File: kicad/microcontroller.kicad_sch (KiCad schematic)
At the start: 26 parts, among them Q701 DMG1012T, U701 MLPF-WB55-01E3, U702 STM32WB55RGVx, Y701 32M

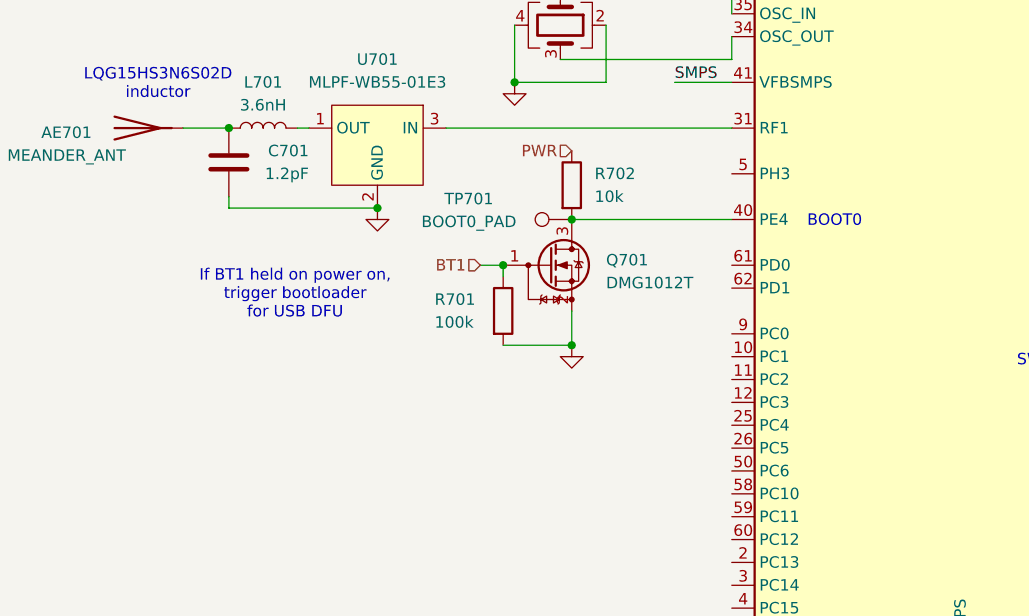
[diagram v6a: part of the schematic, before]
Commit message: Update BOOT0
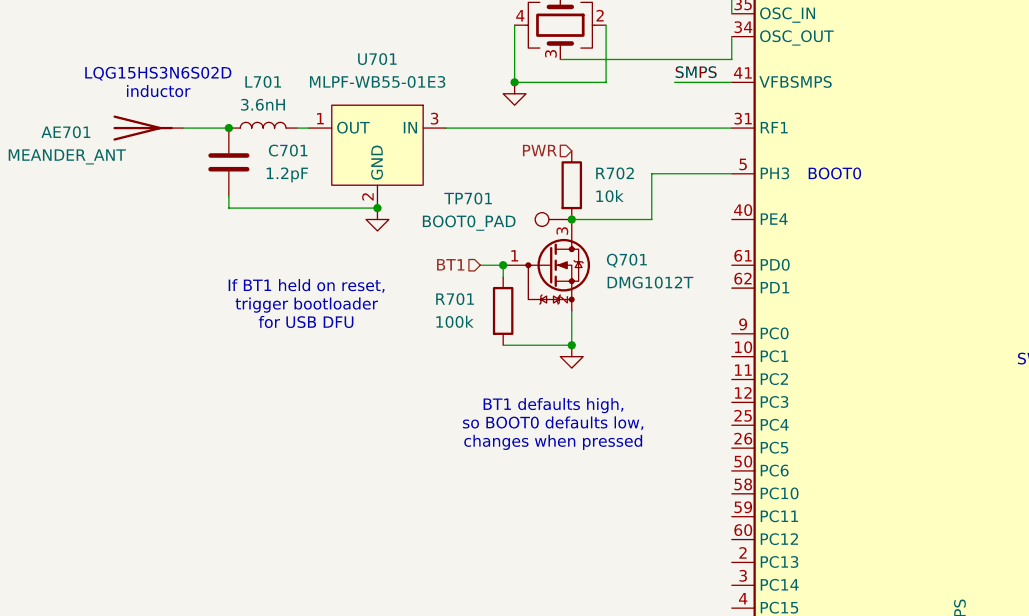
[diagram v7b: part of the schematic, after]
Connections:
- net at Q701.3 (D), R702.2, TP701.1: now also U702.5 (PH3); no longer U702.40 (PE4)
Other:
- note added: "BT1 defaults high, so BOOT0 defaults low, changes when pressed"
- note added: "If BT1 held on reset, trigger bootloader for USB DFU"
- note removed: "If BT1 held on power on, trigger bootloader for USB DFU"
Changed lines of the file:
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@@
+	(wire
+		(pts
+			(xy 106.68 104.14) (xy 106.68 109.22)
+		)
+		(stroke
+			(width 0)
+			(type default)
+		)
+	)
 	(wire
 		(pts
@@
 	(wire
 		(pts
-			(xy 97.79 109.22) (xy 115.57 109.22)
-		)
-		(stroke
-			(width 0)
-			(type default)
-		)
-	)
-	(wire
-		(pts
 			(xy 109.22 78.74) (xy 115.57 78.74)
 		)
@@
 	(wire
 		(pts
+			(xy 115.57 104.14) (xy 106.68 104.14)
+		)
+		(stroke
+			(width 0)
+			(type default)
+		)
+	)
+	(wire
+		(pts
 			(xy 158.75 119.38) (xy 162.56 119.38)
 		)
@@
 	(wire
 		(pts
+			(xy 106.68 109.22) (xy 97.79 109.22)
+		)
+		(stroke
+			(width 0)
+			(type default)
+		)
+	)
+	(wire
+		(pts
 			(xy 82.55 71.12) (xy 76.2 71.12)
 		)
@@
 		)
 	)
-	(text "LQG15HS3N6S02D\ninductor\n"
-		(exclude_from_sim no)
-		(at 51.816 94.234 0)
+	(text "BT1 defaults high,\nso BOOT0 defaults low,\nchanges when pressed"
+		(exclude_from_sim no)
+		(at 95.758 132.08 0)
 		(effects
 			(font
@@
 		)
 	)
-	(text "If BT1 held on power on,\ntrigger bootloader\nfor USB DFU"
-		(exclude_from_sim no)
-		(at 67.056 117.602 0)
+	(text "LQG15HS3N6S02D\ninductor\n"
+		(exclude_from_sim no)
+		(at 51.816 94.234 0)
 		(effects
 			(font
@@
 		)
 	)
-	(text "SWO"
-		(exclude_from_sim no)
-		(at 149.352 124.968 0)
+	(text "If BT1 held on reset,\ntrigger bootloader\nfor USB DFU"
+		(exclude_from_sim no)
+		(at 68.326 118.872 0)
 		(effects
 			(font
@@
 		)
 	)
-	(text "LRA PWM"
-		(exclude_from_sim no)
-		(at 180.594 73.914 0)
+	(text "SWO"
+		(exclude_from_sim no)
+		(at 149.352 124.968 0)
 		(effects
 			(font
@@
 		)
 	)
-	(text "SPI1:\nE-Ink display"
-		(exclude_from_sim no)
-		(at 183.642 88.138 0)
+	(text "LRA PWM"
+		(exclude_from_sim no)
+		(at 180.594 73.914 0)
 		(effects
 			(font
@@
 		)
 	)
-	(text "I2C1:\nLRA"
-		(exclude_from_sim no)
-		(at 183.134 138.938 0)
+	(text "SPI1:\nE-Ink display"
+		(exclude_from_sim no)
+		(at 183.642 88.138 0)
 		(effects
 			(font
@@
 		)
 	)
+	(text "I2C1:\nLRA"
+		(exclude_from_sim no)
+		(at 183.134 138.938 0)
+		(effects
+			(font
+				(size 1.27 1.27)
+			)
+		)
+	)
 	(text "BOOT0"
 		(exclude_from_sim no)
-		(at 127 109.474 0)
-		(effects
-			(font
+		(at 127 104.394 0)
+		(effects
+			(font

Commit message: v2.0.1
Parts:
- removed TP701: BOOT0_PAD, TestPoint:TestPoint_Pad_D1.0mm, symbol Connector:TestPoint
- removed TP703: FLASH_GND, TestPoint:TestPoint_Pad_D1.0mm, symbol Connector:TestPoint
- removed TP704: FLASH_DIO, TestPoint:TestPoint_Pad_D1.0mm, symbol Connector:TestPoint
- removed TP705: FLASH_CLK, TestPoint:TestPoint_Pad_D1.0mm, symbol Connector:TestPoint
- removed TP706: FLASH_RST, TestPoint:TestPoint_Pad_D1.0mm, symbol Connector:TestPoint
- removed TP707: FLASH_VDD, TestPoint:TestPoint_Pad_D1.0mm, symbol Connector:TestPoint
- added C713: 100nF, Capacitor_SMD:C_0402_1005Metric, symbol Device:C
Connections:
- net GND: now also C713.1
- net NRST: no longer names the net of U702.8 (NRST)
- net NRST: now also C713.2
- net SWCLK: no longer names the net of U702.56 (PA14)
- net SWDIO: no longer names the net of U702.54 (PA13)
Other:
- note added: "SWCLK"
- note added: "SWDIO"
